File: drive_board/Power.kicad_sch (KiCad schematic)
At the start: 0 parts

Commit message: Ethernet ish and Megafit
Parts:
- added D1: LED, MRDT_Connectors:MOLEX_MegaFit_02_Horizontal, symbol Device:LED
- added J1: Molex_Megafit_02, MRDT_Connectors:MOLEX_MegaFit_02_Horizontal, symbol MRDT_Connectors:Molex_Megafit_02
- added R1: 2.2k, symbol Device:R_US
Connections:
- new net: D1.1 (K), R1.1
- new net +24V: D1.2 (A), J1.2
- new net GND: J1.1, R1.2

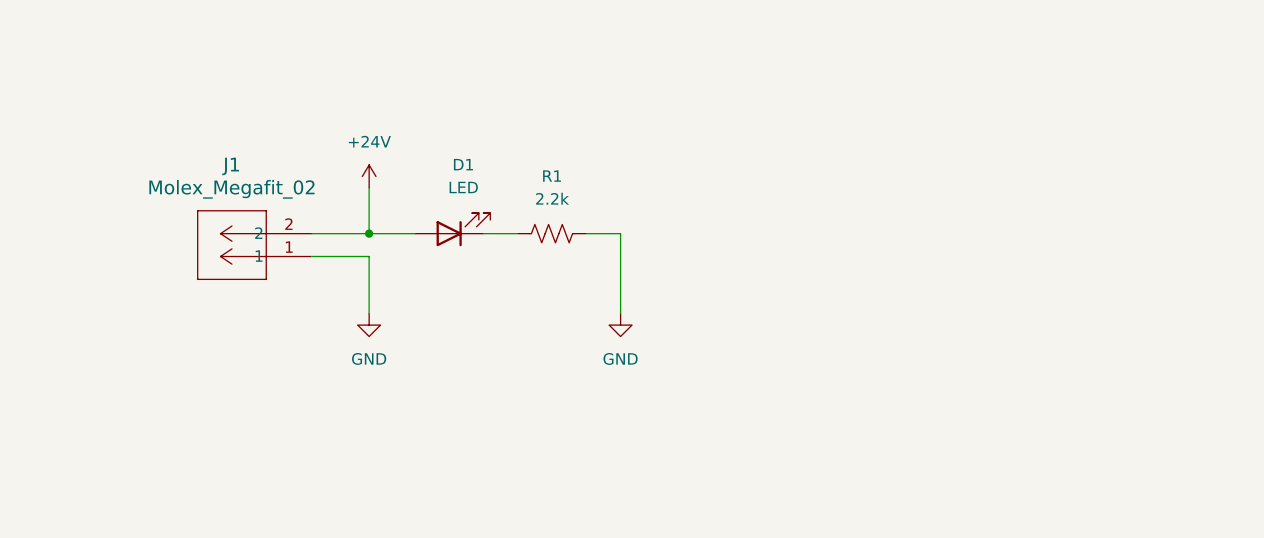
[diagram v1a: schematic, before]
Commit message: New Stuff
- Reverse voltage protection
- D-Pad for test buttons
- Rotary encoder for test buttons
- Finished ethernet circuit
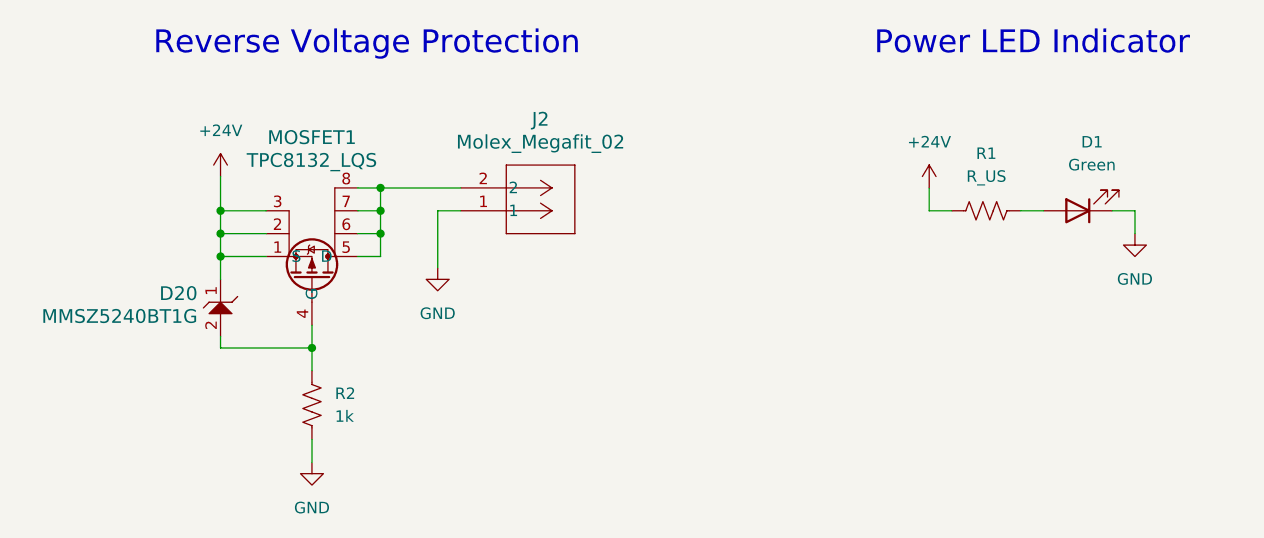
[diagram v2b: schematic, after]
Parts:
- removed J1: Molex_Megafit_02, MRDT_Connectors:MOLEX_MegaFit_02_Horizontal, symbol MRDT_Connectors:Molex_Megafit_02
- added D20: MMSZ5240BT1G, MRDT_Devices:SOD-123_ONS-L, symbol MRDT_Devices:MMSZ5240BT1G
- added J2: Molex_Megafit_02, MRDT_Connectors:MOLEX_MegaFit_02_Horizontal, symbol MRDT_Connectors:Molex_Megafit_02
- added MOSFET1: TPC8132_LQS, Package_SO:SOIC-8_3.9x4.9mm_P1.27mm, symbol MRDT_Devices:TPC8132_LQS
- added R2: 1k, symbol Device:R_US
- D1: value LED -> Green; footprint MRDT_Connectors:MOLEX_MegaFit_02_Horizontal -> (none)
- R1: value 2.2k -> R_US
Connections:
- net +24V: now also R1.1, D20.1, MOSFET1.1 (S), MOSFET1.2, MOSFET1.3; no longer D1.2 (A)
- net GND: now also D1.1 (K), J2.1, R2.2; no longer R1.2
- new net: D20.2, MOSFET1.4 (G), R2.1
- new net: J2.2, MOSFET1.5 (D), MOSFET1.6, MOSFET1.7, MOSFET1.8
- new net: D1.2 (A), R1.2
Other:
- note added: "Power LED Indicator"
- note added: "Reverse Voltage Protection"

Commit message: Even More New Stuff
- CAN Transceiver
- Global and hierarchal labels
- How the heck does the rotary encoder work? Lmk when I'm in the office.
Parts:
- R1: value R_US -> 3.3k

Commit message: Finish schematic
- Finished requirements
- Cleaned up and organized some stuff
- Can still clean up a little more
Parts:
- R2: renamed from R1; value 3.3k -> 6.8k
- renumbered D20 to D1, D1 to D2, J2 to J1, R2 to R1

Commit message: Organize schematic stuff
- Did new stuff lol!1! 67
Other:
- note added: "white space lol"
- moved on the sheet: D1, D2, J1, MOSFET1, R1, R2

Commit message: Adjust according to schematic review
- Added some pull down resistors and such
- Lowkey forgot because I forgot to commit and am a couple days late.
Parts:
- added C2: 0.1 uF, symbol Device:C
- added D15: Green, symbol Device:LED
- added R23: 6.8k, symbol Device:R_US
- R1: value 1k -> 10k
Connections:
- net +24V: now also C2.1
- net GND: now also D15.1 (K)
- net at D1.2, MOSFET1.4 (G), R1.1: now also C2.2
- new net: D15.2 (A), R23.2
- new net +3V3: R23.1
